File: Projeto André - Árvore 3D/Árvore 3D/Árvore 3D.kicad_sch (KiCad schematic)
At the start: 58 parts, among them J1 Conn_01x03_Pin, J10 TestPoint, J11 TestPoint, J12 TestPoint, J13 TestPoint, J14 TestPoint, J15 TestPoint, J16 TestPoint, J17 TestPoint, J18 TestPoint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

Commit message: Revisão do projeto e inclusão de logos.
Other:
- moved on the sheet: C5, R1, R10, R11, R12, R13, R14, R15, R16, R17, R2, R3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

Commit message: Finalização da versão inicial - Rev.00
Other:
- title: Árvore de Natal 3D -> Projeto Natal 2023 - Árvore de Natal 3D
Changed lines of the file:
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@@
   (paper "A4")
   (title_block
-    (title "Árvore de Natal 3D")
+    (title "Projeto Natal 2023 - Árvore de Natal 3D")
     (date "2023-11-17")
     (rev "00")

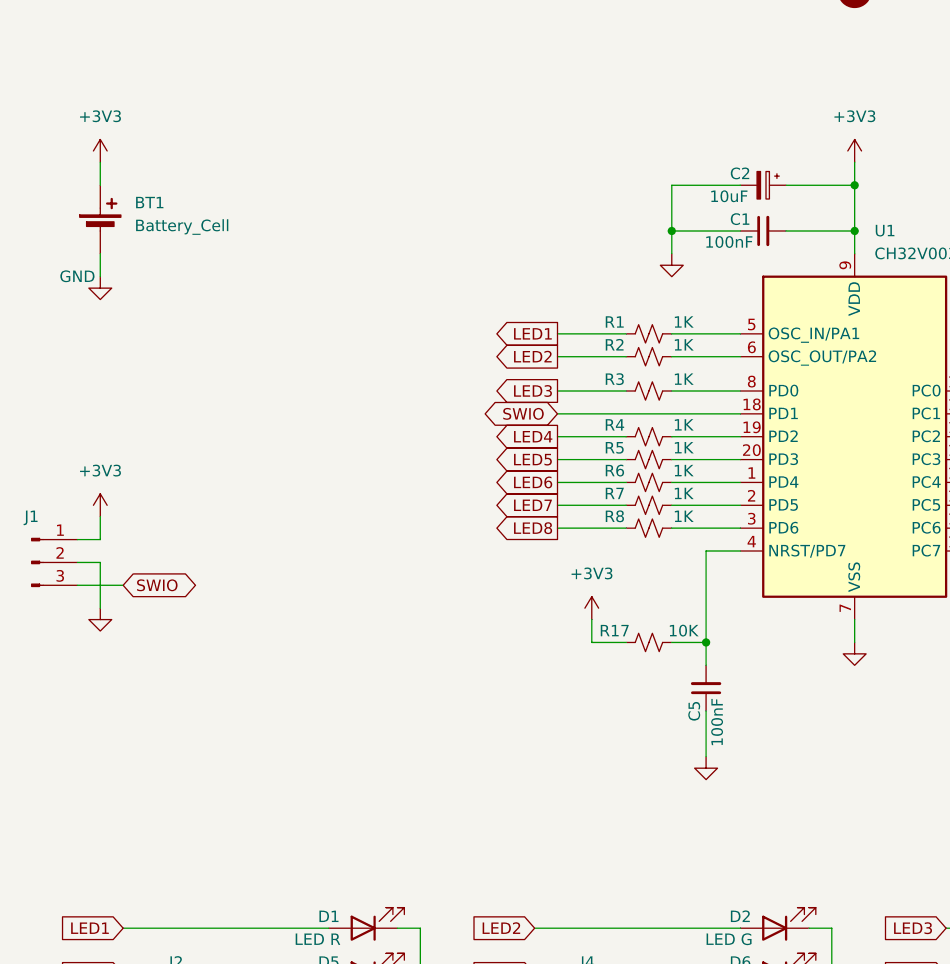
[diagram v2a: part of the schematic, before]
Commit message: Início da Rev.01. Inclusão de Test Points. Inclusão de botão e inclusão do arquivo 3D do suporte de bateria. Melhorias gerais.
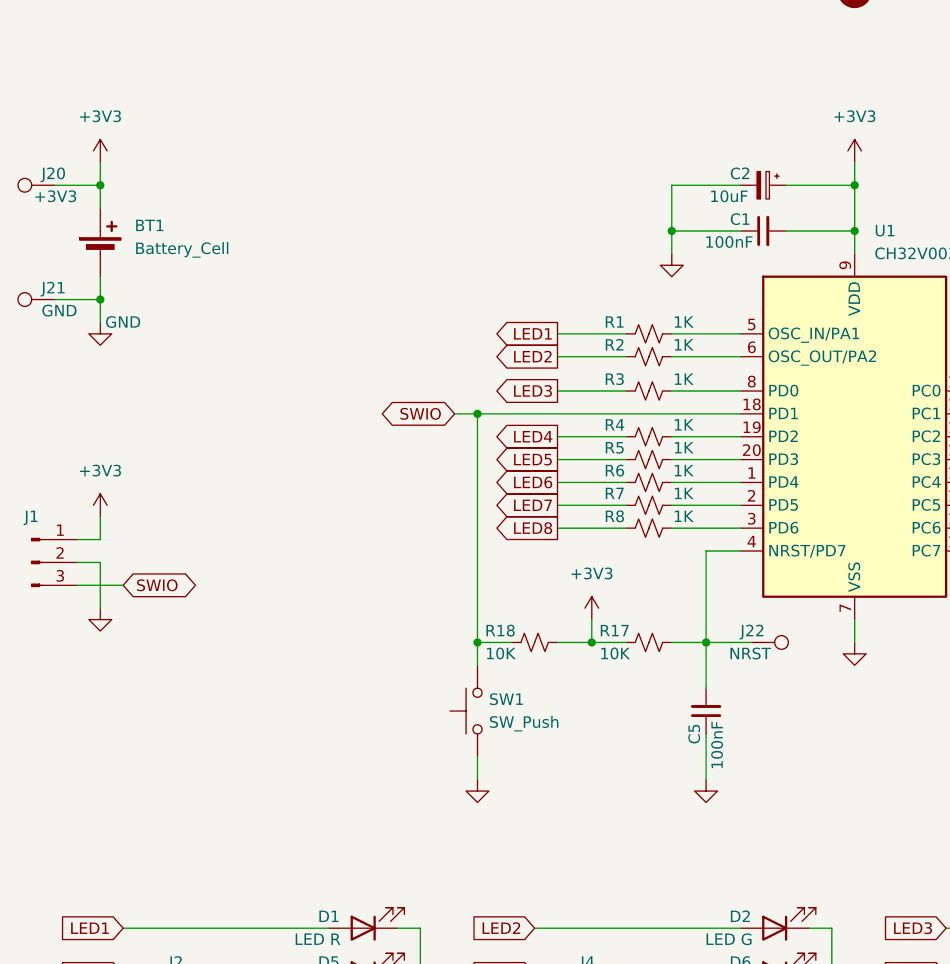
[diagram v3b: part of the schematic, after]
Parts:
- added J20: +3V3, TestPoint:TestPoint_THTPad_D1.5mm_Drill0.7mm, symbol Connector:TestPoint
- added J21: GND, TestPoint:TestPoint_THTPad_D1.5mm_Drill0.7mm, symbol Connector:TestPoint
- added J22: NRST, TestPoint:TestPoint_THTPad_D1.5mm_Drill0.7mm, symbol Connector:TestPoint
- added R18: 10K, Resistor_SMD:R_0603_1608Metric_Pad0.98x0.95mm_HandSolder, symbol Device:R_Small_US
- added SW1: SW_Push, Button_Switch_SMD:SW_Push_1P1T_NO_6x6mm_H9.5mm, symbol Switch:SW_Push
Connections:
- net +3V3: now also J20.1, R18.2
- net GND: now also J21.1, SW1.1
- net SWIO: now also R18.1, SW1.2
- net at C5.2, R17.2, U1.4 (NRST/PD7): now also J22.1
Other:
- moved on the sheet: BT1, C5

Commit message: Finalização da Rev.01. Elaboração de arquivos de fabricação.
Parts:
- SW1: footprint Button_Switch_SMD:SW_Push_1P1T_NO_6x6mm_H9.5mm -> Button_Switch_SMD:SW_Push_1P1T_NO_CK_KSC6xxJ
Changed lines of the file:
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@@
   (title_block
     (title "Projeto Natal 2023 - Árvore de Natal 3D")
-    (date "2023-11-20")
+    (date "2023-11-21")
     (rev "01")
     (company "Franzininho / Mechatronix Lab")
@@
       (effects (font (size 1.27 1.27)) (justify right))
     )
-    (property "Footprint" "Button_Switch_SMD:SW_Push_1P1T_NO_6x6mm_H9.5mm" (at 104.14 105.41 0)
-      (effects (font (size 1.27 1.27)) hide)
-    )
+    (property "Footprint" "Button_Switch_SMD:SW_Push_1P1T_NO_CK_KSC6xxJ" (at 104.14 105.41 0)
+      (effects (font (size 1.27 1.27)) hide)
+    )
